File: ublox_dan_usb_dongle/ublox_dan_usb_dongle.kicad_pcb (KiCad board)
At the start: 6 copper layers, 43.5 x 22 mm, 19 parts, among them J1 USB_A, J2 USB_A, J3 U.Fl, J4 EXT, U1 DAN-F10N, U2 CH340N, U3 MIC5365-2.85YC5, U4 USBLC6-2SC6, U5 MIC5365-3.3YC5

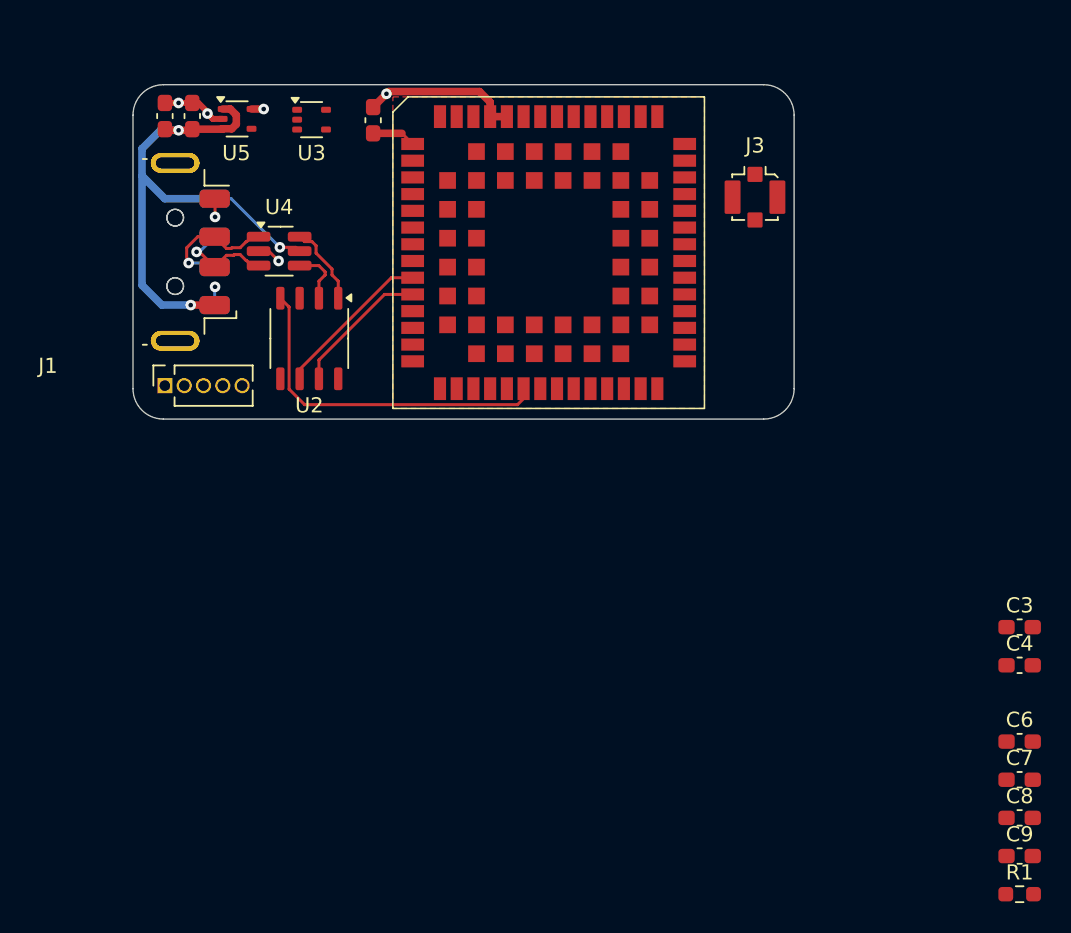
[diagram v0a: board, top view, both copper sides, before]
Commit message: Update gitignore and finish USB GNSS dongle
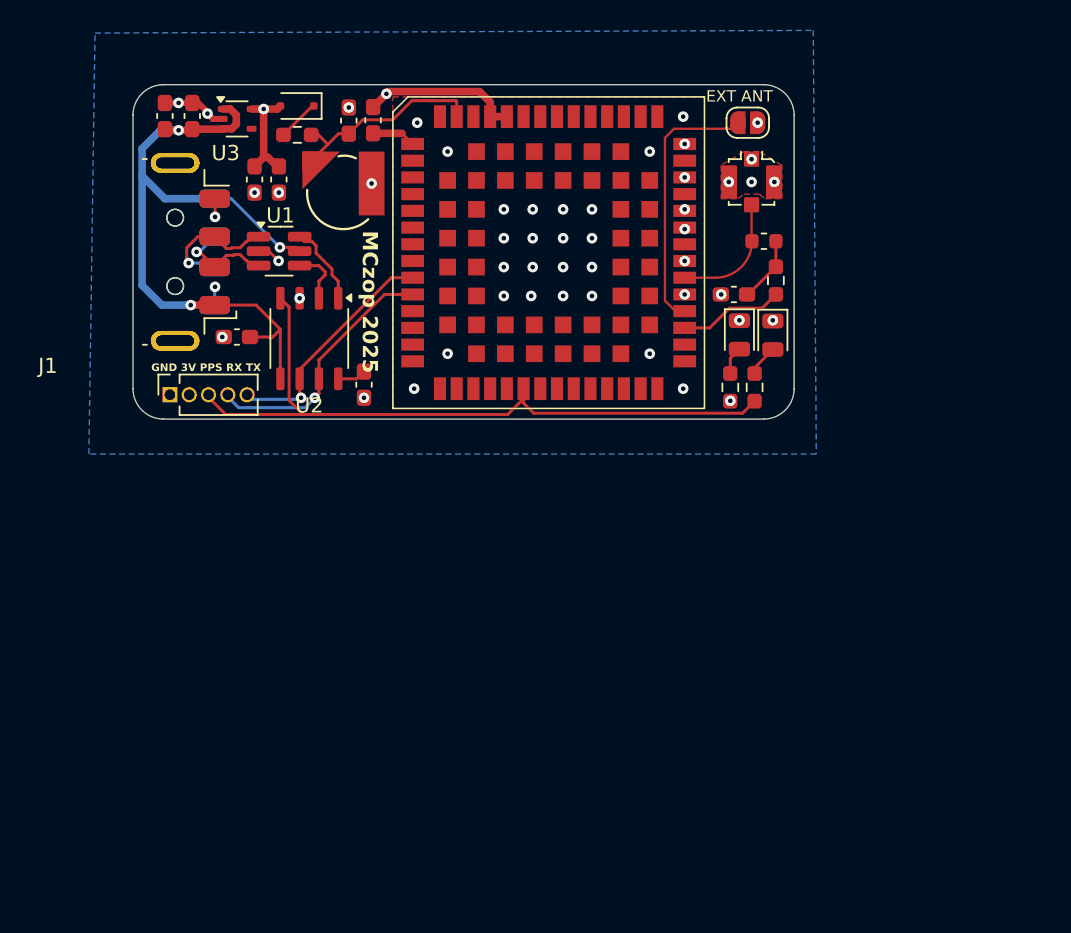
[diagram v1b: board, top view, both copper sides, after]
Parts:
- removed the C4 at (180.9, 117.2)
- removed the C6 at (180.9, 122.2)
- removed the C8 at (180.9, 127.2)
- removed the U3 at (134.3, 81.3)
- added BT1: ML414H, ML414H:ML414H_IV01E, F.Cu at (136.4, 86.1)
- added C1: 4.7u, Capacitor_SMD:C_0603_1608Metric_Pad1.08x0.95mm_HandSolder, F.Cu at (136.8, 81.4)
- added C2: 100n, Capacitor_SMD:C_0603_1608Metric_Pad1.08x0.95mm_HandSolder, F.Cu at (137.8, 98.7)
- added C5: 100n, Capacitor_SMD:C_0603_1608Metric_Pad1.08x0.95mm_HandSolder, F.Cu at (162.1, 92.8)
- added D1: PMEG4005EJ, Diode_SMD:D_SOD-323F, F.Cu at (133.4, 80.4)
- added D2: Red, LED_SMD:LED_0805_2012Metric, F.Cu at (162.5, 95.5)
- added D3: Grrer, LED_SMD:LED_0805_2012Metric, F.Cu at (164.7, 95.5)
- added JP1: EXT_ANT, Jumper:SolderJumper-2_P1.3mm_Open_RoundedPad1.0x1.5mm, F.Cu at (163.1, 81.5)
- added L1: 27nH, Inductor_SMD:L_0603_1608Metric, F.Cu at (164.1, 89.3)
- added R2: 10, Resistor_SMD:R_0603_1608Metric_Pad0.98x0.95mm_HandSolder, F.Cu at (164.9, 91.9)
- added R3: 5.1k, Resistor_SMD:R_0603_1608Metric_Pad0.98x0.95mm_HandSolder, F.Cu at (161.9, 98.9)
- added R4: 470, Resistor_SMD:R_0603_1608Metric_Pad0.98x0.95mm_HandSolder, F.Cu at (163.5, 98.9)
- C3: value 4.7u -> 100n
- R1: value R_Small -> 1k
- moved R1 69.0 mm to (133.4, 82.3), turned to 180 degrees
- moved C9 67.2 mm to (130.6, 85.2), turned to -90 degrees
- moved C7 62.7 mm to (132.2, 85.2), turned to -90 degrees
- moved C3 54.9 mm to (129.4, 95.6), turned to 180 degrees
- moved J3 1.02 mm to (163.3, 85.4)
- moved J4 0.68 mm to (125.0, 99.4)
- renumbered C2 to C4, C1 to C6, C5 to C8, U4 to U1, U5 to U3, U1 to U4
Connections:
- C3 pad 1: +3V3 -> VBUS
- C7 pad 1: VBUS -> +3V3
- C9 pad 1: +BATT -> +3V3
- J3 pad 1: unconnected-(J3-In-Pad1) -> /RFIN
- J3 pad 2: unconnected-(J3-Ext-Pad2) -> GND
- J4 pad 1: unconnected-(J4-Pin_1-Pad1) -> GND
- J4 pad 2: unconnected-(J4-Pin_2-Pad2) -> +3V3
- J4 pad 3: unconnected-(J4-Pin_3-Pad3) -> /PPS
- J4 pad 4: unconnected-(J4-Pin_4-Pad4) -> /CRX
- J4 pad 5: unconnected-(J4-Pin_5-Pad5) -> /CTX
- R1 pad 1: unconnected-(R1-Pad1) -> V_BCKP
- R1 pad 2: unconnected-(R1-Pad2) -> Net-(D1-K)
- U2 pad 5: unconnected-(U2-VCC-Pad5) -> VBUS
- U2 pad 8: unconnected-(U2-V3-Pad8) -> Net-(U2-V3)
- U4 pad 31: unconnected-(U1-VCC_RF-Pad31) -> /RF_VCC
- U4 pad 32: unconnected-(U1-ANT_CTRL-Pad32) -> /EXT_ANT
- U4 pad 34: unconnected-(U1-EXT_RF_IN-Pad34) -> /RFIN
- U4 pad 55: unconnected-(U1-V_BCKP-Pad55) -> V_BCKP
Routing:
- net /PPS: track 22.9 -> 47.5 mm
- net /EXT_ANT: track 0.00 -> 17.5 mm
- net V_BCKP: track 0.00 -> 13.6 mm
- net VBUS: track 36.2 -> 47.1 mm
- net /RFIN: track 0.00 -> 8.11 mm
- net /CRX: track 9.19 -> 17.0 mm, vias 0 -> 1
- net /RF_VCC: track 0.00 -> 6.91 mm
- net +3V3: track 11.3 -> 17.7 mm, vias 2 -> 4
- net /CTX: track 10.8 -> 15.8 mm, vias 0 -> 1
- net Net-(C5-Pad1): track 0.00 -> 4.33 mm
- net Net-(D1-K): track 0.00 -> 2.79 mm
- net Net-(D3-A): track 0.00 -> 2.07 mm
- net Net-(U2-V3): track 0.00 -> 1.89 mm
- net Net-(D2-A): track 0.00 -> 1.85 mm
- net GND: vias 5 -> 49
- added copper zone on B.Cu, net GND
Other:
- board text added: "EXT ANT"
- board text added: "GND 3V PPS RX TX"
- board text added: "MCzop 2025"
- board text added: "Ublox DAN-F10N USB dongle"
